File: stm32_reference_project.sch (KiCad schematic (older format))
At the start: 4 parts

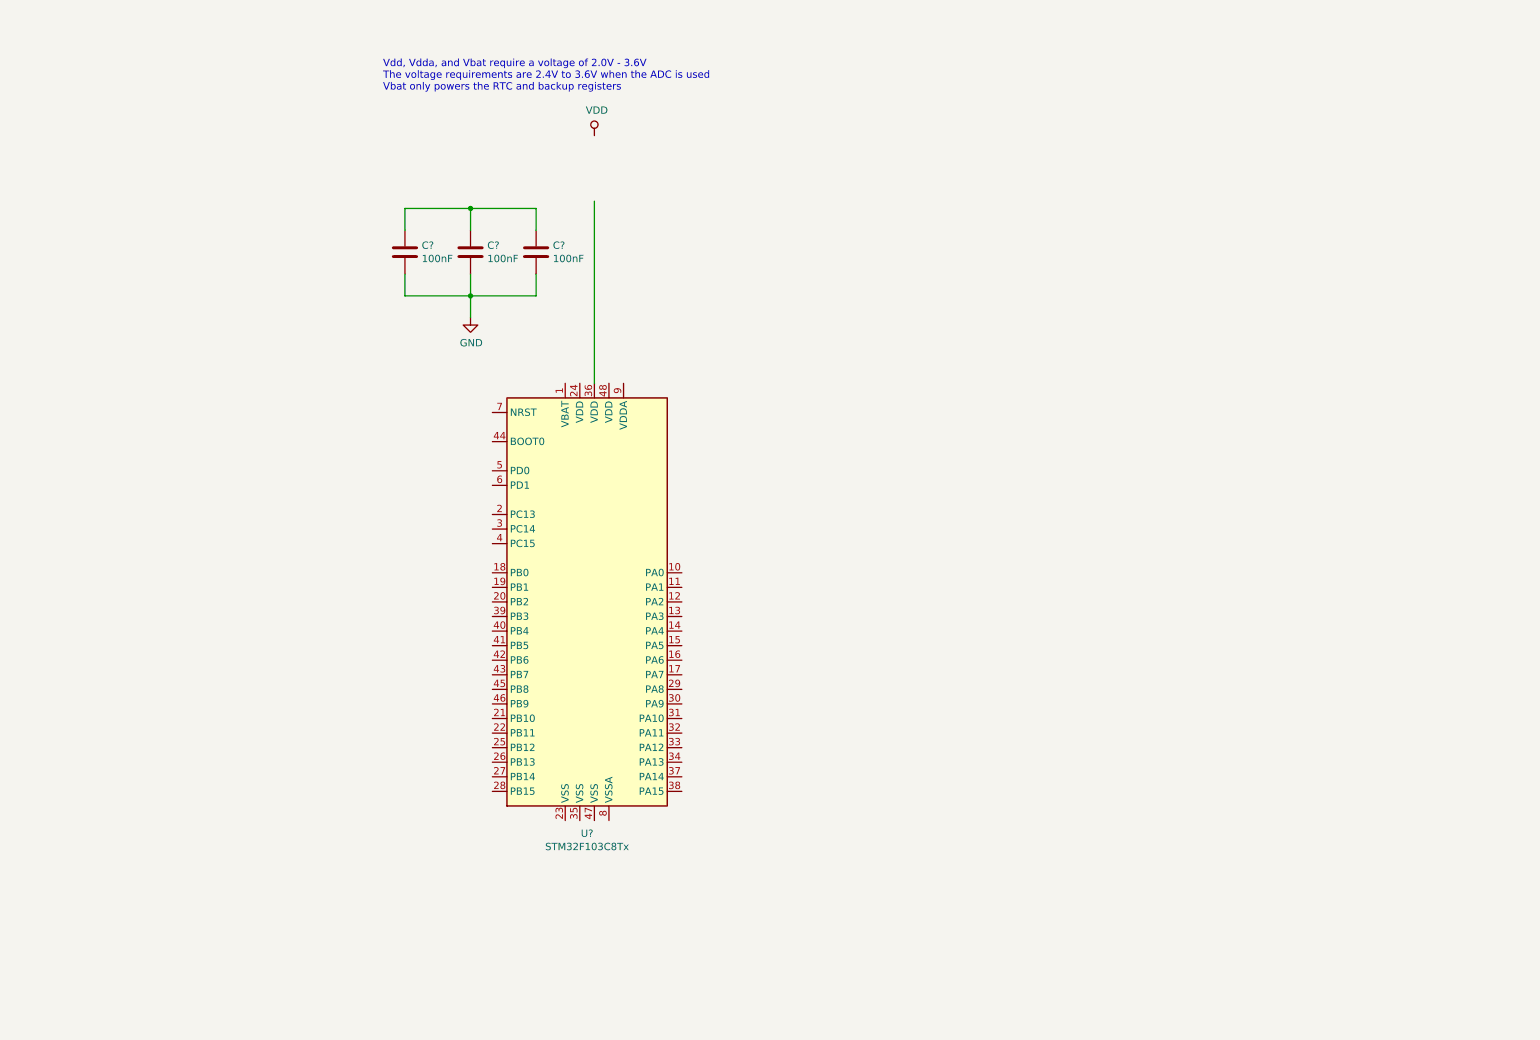
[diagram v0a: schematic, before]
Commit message: Mostly finish the circuit, power regulation needs some love
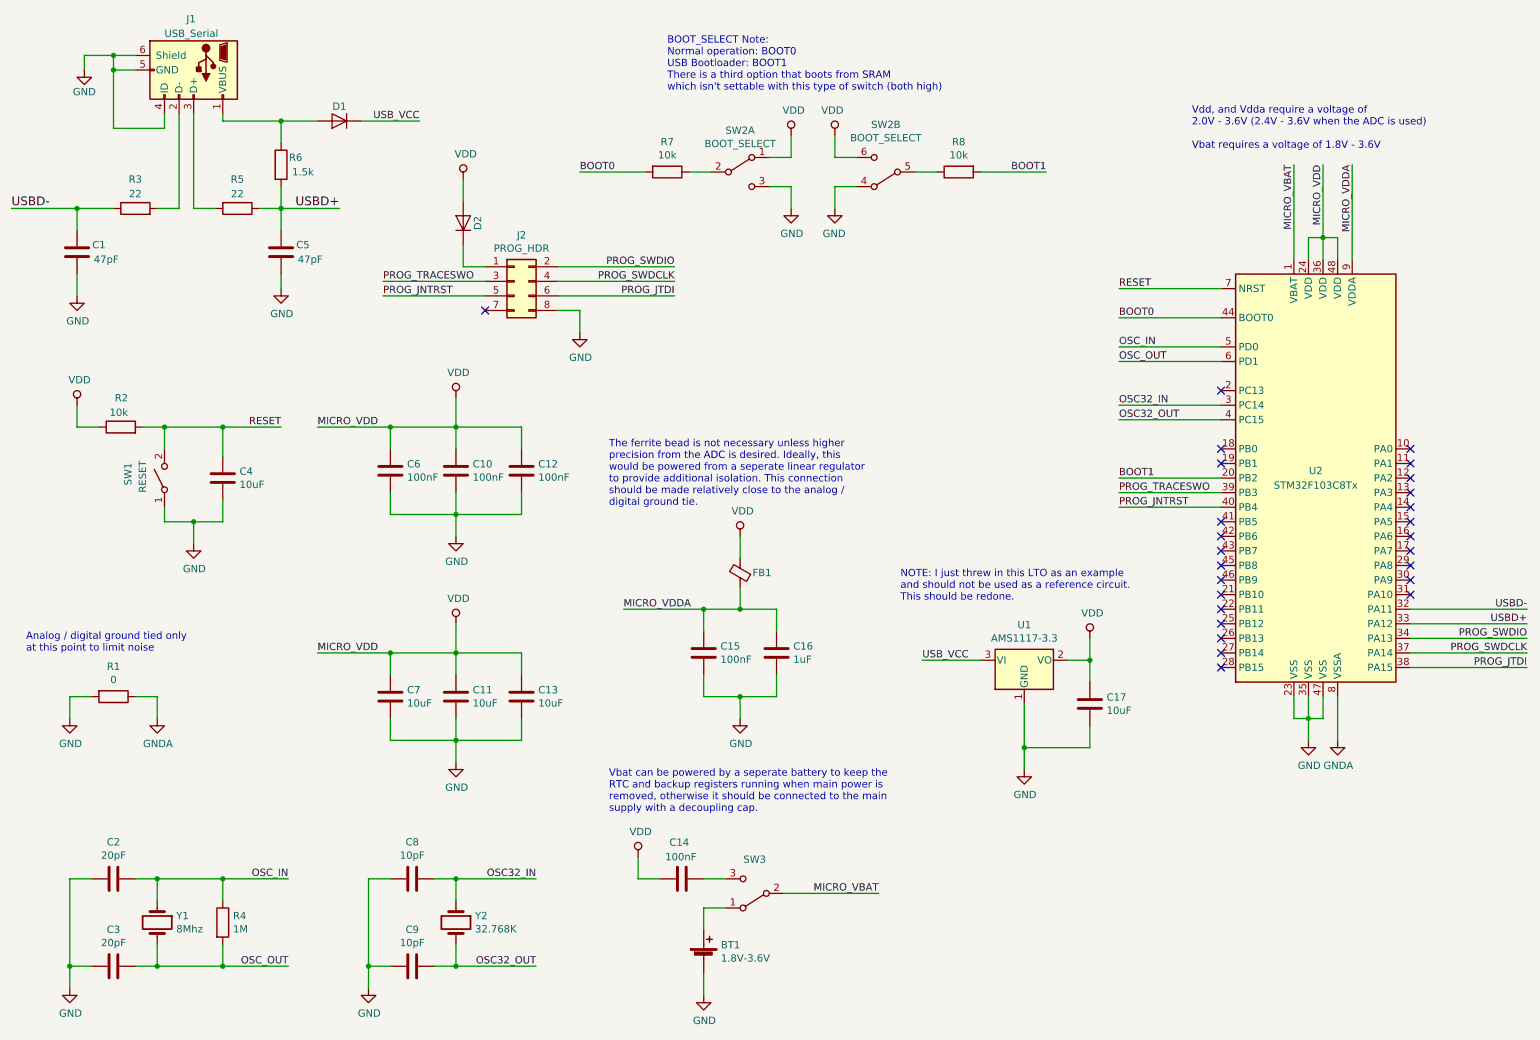
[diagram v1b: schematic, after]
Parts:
- added BT1: 1.8V-3.6V, Battery:Battery_CR1225, symbol Device:Battery_Cell
- added C1, C5: 47pF, Capacitor_SMD:C_0603_1608Metric, symbol Device:C
- added C11, C13, C17, C4, C7: 10uF, Capacitor_SMD:C_0603_1608Metric, symbol Device:C
- added C14, C15: 100nF, Capacitor_SMD:C_0603_1608Metric, symbol Device:C
- added C16: 1uF, Capacitor_SMD:C_0603_1608Metric, symbol Device:C
- added C2, C3: 20pF, Capacitor_SMD:C_0603_1608Metric, symbol Device:C
- added C8, C9: 10pF, Capacitor_SMD:C_0603_1608Metric, symbol Device:C
- added D1, D2: 12V, Diode_SMD:D_SOD-123, symbol Device:D
- added FB1: PowerLine 220 Ohms @ 100MHz (Value unclear), Resistor_SMD:R_0603_1608Metric, symbol Device:Ferrite_Bead_Small
- added J1: USB_Serial, Connector_USB:USB_Micro-B_Wuerth_629105150521, symbol relay_system_controller-rescue:USB_OTG-relay_system_controller-rescue
- added J2: PROG_HDR, Connector_PinHeader_2.54mm:PinHeader_2x05_P2.54mm_Vertical, symbol Connector_Generic:Conn_02x04_Odd_Even
- added R1: 0, Resistor_SMD:R_0603_1608Metric, symbol Device:R
- added R2, R7, R8: 10k, Resistor_SMD:R_0603_1608Metric, symbol Device:R
- added R3, R5: 22, Resistor_SMD:R_0603_1608Metric, symbol relay_system_controller-rescue:R-relay_system_controller-rescue
- added R4: 1M, Resistor_SMD:R_0603_1608Metric, symbol Device:R
- added R6: 1.5k, Resistor_SMD:R_0603_1608Metric, symbol relay_system_controller-rescue:R-relay_system_controller-rescue
- added SW1: RESET, Button_Switch_SMD:SW_SPST_TL3342, symbol Switch:SW_SPST
- added SW2: BOOT_SELECT, Button_Switch_THT:SW_E-Switch_EG1271_DPDT, symbol Switch:SW_DPDT_x2
- added SW3: BAT_SELECT, Button_Switch_SMD:SW_SPDT_CK-JS102011SAQN, symbol Switch:SW_SPDT
- added U1: AMS1117-3.3, Package_TO_SOT_SMD:SOT-223-3_TabPin2, symbol Regulator_Linear:AMS1117-3.3
- added Y1: 8Mhz, Crystal:Crystal_SMD_HC49-SD, symbol Device:Crystal
- added Y2: 32.768K, Capacitor_SMD:C_1206_3216Metric_Pad1.42x1.75mm_HandSolder, symbol Device:Crystal
- gave numbers to parts that had none: 4
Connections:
- net labels added: BOOT0, BOOT1, GNDA, MICRO_VBAT, MICRO_VDD, MICRO_VDDA, OSC32_IN, OSC32_OUT, OSC_IN, OSC_OUT, PROG_JNTRST, PROG_JTDI, PROG_SWDCLK, PROG_SWDIO, PROG_TRACESWO, RESET, USBD+, USBD-, USB_VCC
- wire segments 12 -> 170
- no-connect marks 0 -> 26
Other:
- note added: "Analog / digital ground tied only\nat this point to limit noise"
- note added: "BOOT_SELECT Note:\nNormal operation: BOOT0\nUSB Bootloader: BOOT1\nThere is a third option that boots from SRAM\nwhich isn't settable with this type of switch (both high)"
- note added: "NOTE: I just threw in this LTO as an example\nand should not be used as a reference circuit.\nThis should be redone."
- note added: "The ferrite bead is not necessary unless higher\nprecision from the ADC is desired. Ideally, this\nwould be powered from a seperate linear regulator\nto provide additional isolation. This connection\nshould be made relatively close to the analog /\ndigital ground tie."
- note added: "Vbat can be powered by a seperate battery to keep the\nRTC and backup registers running when main power is\nremoved, otherwise it should be connected to the main\nsupply with a decoupling cap."
- note added: "Vdd, and Vdda require a voltage of\n2.0V - 3.6V (2.4V - 3.6V when the ADC is used)\n\nVbat requires a voltage of 1.8V - 3.6V"
- note removed: "Vdd, Vdda, and Vbat require a voltage of 2.0V - 3.6V\nThe voltage requirements are 2.4V to 3.6V when the ADC is used\nVbat only powers the RTC and backup registers"
- moved on the sheet: C10, C12, C6, U2

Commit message: Commit some updates I forgot about
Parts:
- removed R2: 10k, Resistor_SMD:R_0603_1608Metric, symbol Device:R
- C1, C5: Spice_Model (none) -> 47p; Spice_Netlist_Enabled (none) -> Y; Spice_Primitive (none) -> C
- C10, C12, C14, C6: value 100nF -> 0.1uF
- C11, C13, C7: Spice_Model 100n -> 10u
- C15: value 100nF -> 0.1uF; Spice_Model (none) -> 100n; Spice_Netlist_Enabled (none) -> Y; Spice_Primitive (none) -> C
- C16: Spice_Model (none) -> 1u; Spice_Netlist_Enabled (none) -> Y; Spice_Primitive (none) -> C
- C17: Spice_Model (none) -> 10u; Spice_Netlist_Enabled (none) -> Y; Spice_Primitive (none) -> C
- C2, C3: Spice_Model (none) -> 20p; Spice_Netlist_Enabled (none) -> Y; Spice_Primitive (none) -> C
- C4: value 10uF -> 0.1uF; footprint Capacitor_SMD:C_0603_1608Metric -> (none); Spice_Model (none) -> 100nF; Spice_Netlist_Enabled (none) -> Y; Spice_Primitive (none) -> C
- C8, C9: Spice_Model (none) -> 10p; Spice_Netlist_Enabled (none) -> Y; Spice_Primitive (none) -> C
- D1, D2: value 12V -> NEEDS_SPEC
- FB1: value PowerLine 220 Ohms @ 100MHz (Value unclear) -> NEEDS_SPEC
- J1: symbol relay_system_controller-rescue:USB_OTG-relay_system_controller-rescue -> stm32_reference_project-rescue:USB_OTG-relay_system_controller-rescue-relay_system_controller-rescue
- R1: Spice_Model (none) -> 0; Spice_Netlist_Enabled (none) -> Y; Spice_Primitive (none) -> R
- R3, R5: symbol relay_system_controller-rescue:R-relay_system_controller-rescue -> stm32_reference_project-rescue:R-relay_system_controller-rescue-relay_system_controller-rescue; Spice_Model (none) -> 22; Spice_Netlist_Enabled (none) -> Y; Spice_Primitive (none) -> R
- R4: Spice_Model (none) -> 1Meg; Spice_Netlist_Enabled (none) -> Y; Spice_Primitive (none) -> R
- R6: symbol relay_system_controller-rescue:R-relay_system_controller-rescue -> stm32_reference_project-rescue:R-relay_system_controller-rescue-relay_system_controller-rescue; Spice_Model (none) -> 1.5k; Spice_Netlist_Enabled (none) -> Y; Spice_Primitive (none) -> R
- R7, R8: Spice_Model (none) -> 10k; Spice_Netlist_Enabled (none) -> Y; Spice_Primitive (none) -> R
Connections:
- net VDD: now also D2.1 (K); no longer D2.2 (A)
- net at J2.1 (Pin_1): now also D2.2 (A); no longer D2.1 (K)

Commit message: A drunken cleanup
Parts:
- removed U1: AMS1117-3.3, Package_TO_SOT_SMD:SOT-223-3_TabPin2, symbol Regulator_Linear:AMS1117-3.3
- added C?: 1uF, Capacitor_SMD:C_0603_1608Metric, symbol Device:C
- added U?: MIC5501-3.0YM5, Package_TO_SOT_SMD:SOT-23-5, symbol Regulator_Linear:MIC5501-3.0YM5
- C17: value 10uF -> 1uF; Spice_Model 10u -> 1u
- J1: DigiKey Part (none) -> WM11263CT-ND; DigiKey Price (none) -> 0.92
- R1: footprint Resistor_SMD:R_0603_1608Metric -> Resistor_SMD:R_0402_1005Metric; Comment (none) -> DNP / Do Not Populate
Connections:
- net GND: now also C?.2, U?.2 (GND)
- net USB_VCC: now also C?.1, U?.1 (VIN)
- net VDD: now also U?.5 (VOUT)
- no-connect marks 26 -> 27
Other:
- note added: "The ferrite bead is not necessary unless higher\nprecision from the ADC is desired. This connection\nshould be made relatively close to the analog /\ndigital ground tie."
- note added: "Vbat can be powered by a seperate battery to keep the\nRTC and backup registers running when main power is\nremoved, otherwise it should be connected to the main\nsupply with a decoupling cap.\n\nIn real applications a switch should not be used. Temporary\npower loss by actually switching will likely mess up the RTC\nand trip the clock protection circuit which will interrupt and\npotentially halt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"
- note removed: "NOTE: I just threw in this LTO as an example\nand should not be used as a reference circuit.\nThis should be redone."
- note removed: "The ferrite bead is not necessary unless higher\nprecision from the ADC is desired. Ideally, this\nwould be powered from a seperate linear regulator\nto provide additional isolation. This connection\nshould be made relatively close to the analog /\ndigital ground tie."
- note removed: "Vbat can be powered by a seperate battery to keep the\nRTC and backup registers running when main power is\nremoved, otherwise it should be connected to the main\nsupply with a decoupling cap."
- moved on the sheet: BT1, C10, C11, C12, C13, C14, C15, C16, C17, C4, C6, C7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
